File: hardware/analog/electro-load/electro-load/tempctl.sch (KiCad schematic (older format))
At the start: 25 parts, among them M1 Noctua NF-A14 5V, Q1 2N2222A, Q2 2N2222A, U4 LM358DR

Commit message: HW rev 1 of electronic load PCB.
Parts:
- removed R14, R17, R19: 1k, Resistor_SMD:R_0603_1608Metric, symbol Device:R_Small
- removed R15, R16: 10k POT, Potentiometer_SMD:Potentiometer_Bourns_3214W_Vertical, symbol Device:R_Small
- removed R18: 10k, Resistor_SMD:R_0603_1608Metric, symbol Device:R_Small
- removed R20: 3k3, Resistor_SMD:R_0603_1608Metric, symbol Device:R_Small
- removed TP4, TP5, TP8, TP9: TestPoint, athir:testpoint_probe, symbol Connector:TestPoint
- removed U4: LM358DR, digikey-footprints:SOIC-8_W3.9mm, symbol dk_Linear-Amplifiers-Instrumentation-OP-Amps-Buffer-Amps:LM358DR
- added C10, C11, C12, C13: 100n, Capacitor_SMD:C_0603_1608Metric, symbol Device:C_Small
- added R13, R5: 1k, Resistor_SMD:R_0603_1608Metric, symbol Device:R_Small
- added R4: 3k3 1%, Resistor_SMD:R_0603_1608Metric, symbol Device:R_Small
- added RV1, RV2, RV3, RV4: 10k POT, Potentiometer_THT:Potentiometer_Bourns_3296W_Vertical, symbol Device:R_POT
- added U3, U4: LMV321, Package_TO_SOT_SMD:SOT-23-5, symbol Amplifier_Operational:LMV321
- R10: value 10k -> 1k
- R12: value 3k3 -> 10k
- R7: value 10k POT -> 10k; footprint Potentiometer_SMD:Potentiometer_Bourns_3214W_Vertical -> Resistor_SMD:R_0603_1608Metric
- R8: value 10k POT -> 1k; footprint Potentiometer_SMD:Potentiometer_Bourns_3214W_Vertical -> Resistor_SMD:R_0603_1608Metric
- R9: value 1k -> 3k3 1%
- renumbered R13 to R14, TP6 to TP4, TP7 to TP5
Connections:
- wire segments 75 -> 97
- no-connect marks 0 -> 4
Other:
- note removed: "GAIN"

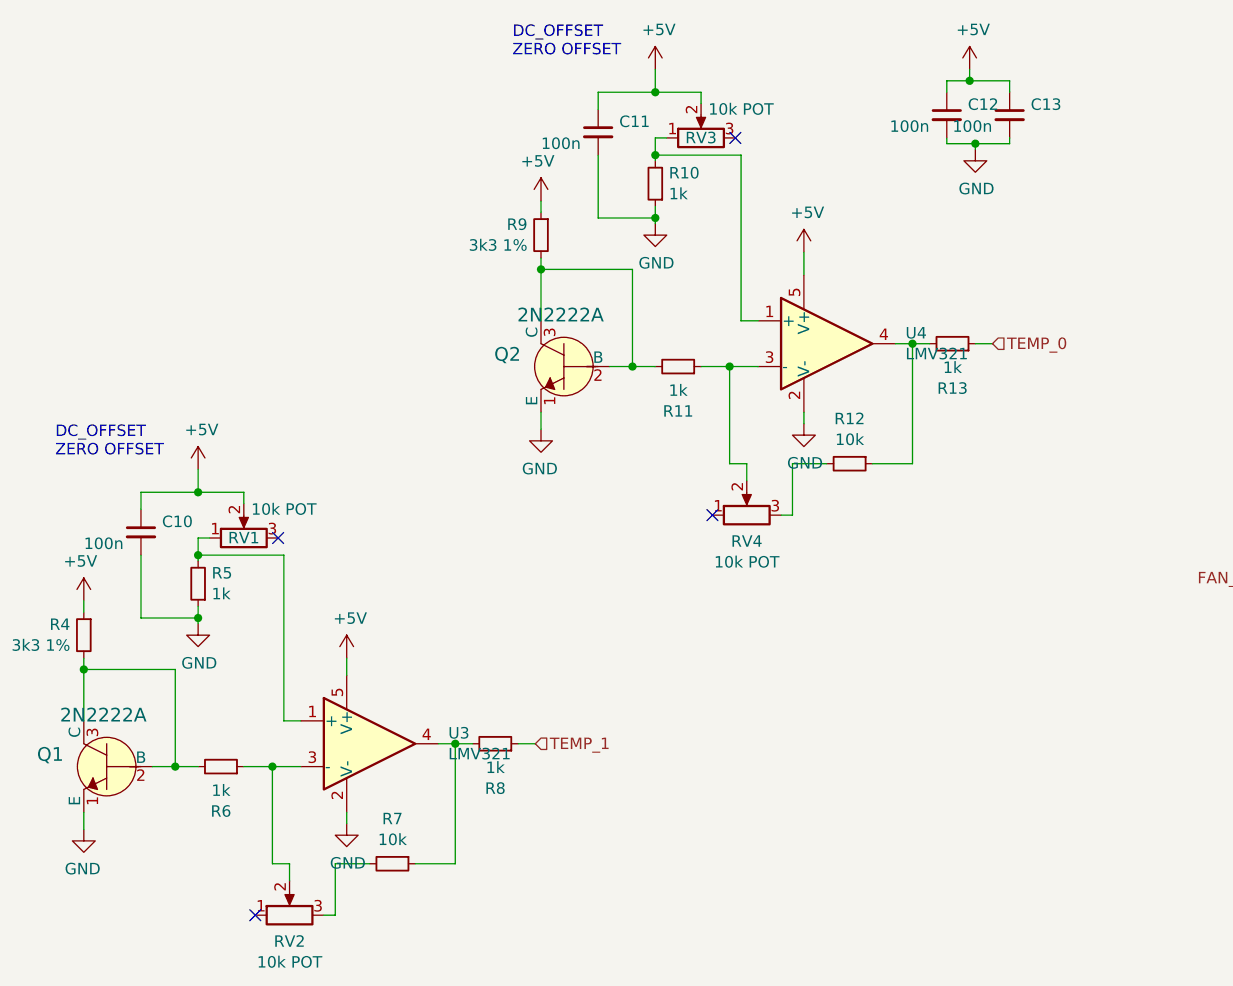
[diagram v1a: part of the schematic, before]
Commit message: Added voltage reference REF5020 datasheet
Started work on HW rev 2 of electro load and 5v-from-mains - rev 1 contained misaligned footprints.
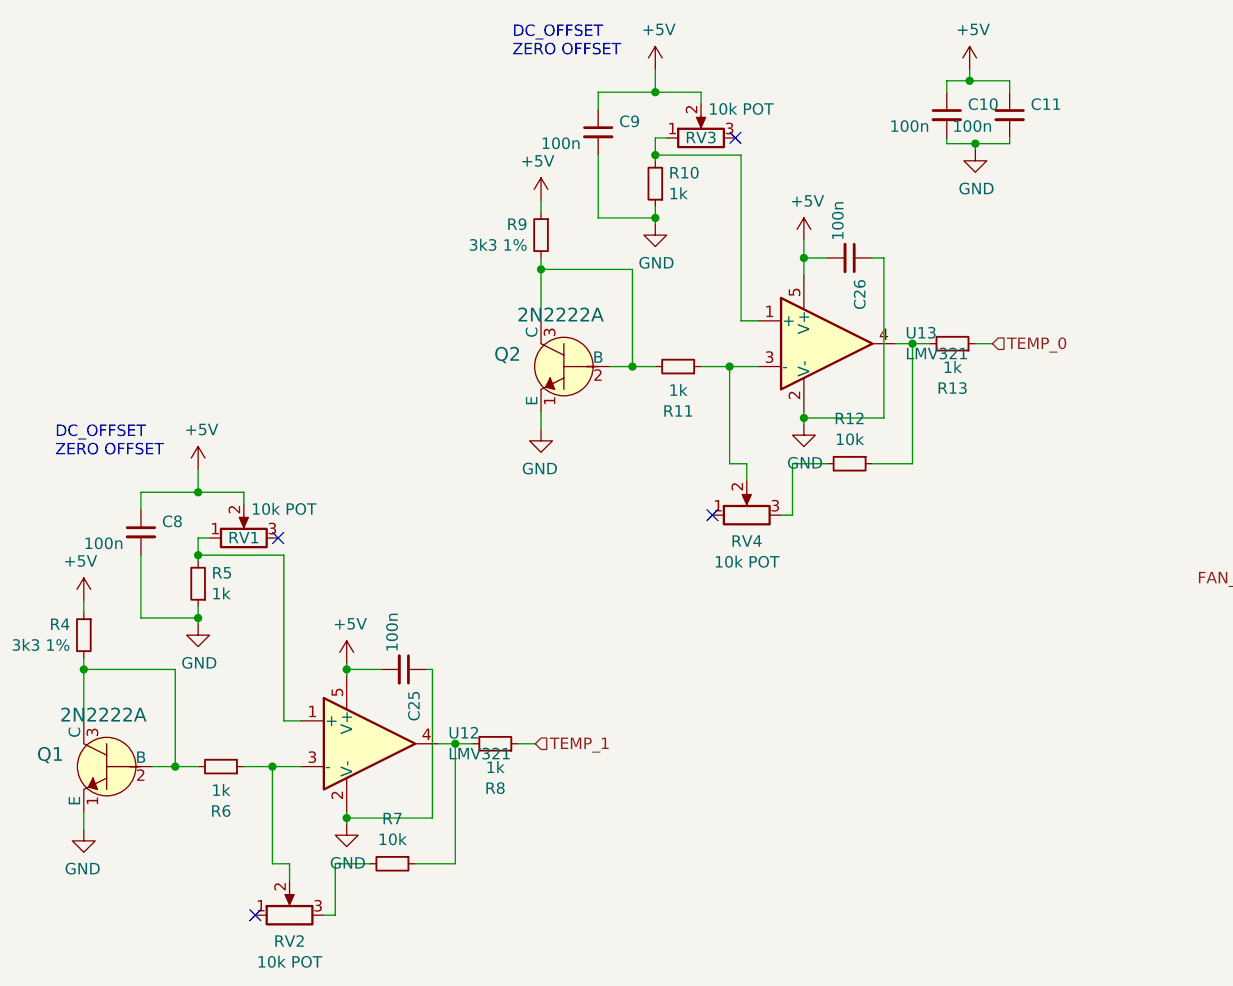
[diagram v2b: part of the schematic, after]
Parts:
- removed U3, U4: LMV321, Package_TO_SOT_SMD:SOT-23-5, symbol Amplifier_Operational:LMV321
- added C25, C26: 100n, Capacitor_SMD:C_0603_1608Metric, symbol Device:C_Small
- added U12, U13: LMV321, Package_TO_SOT_SMD:SOT-23-5, symbol Amplifier_Operational:LMV321
- renumbered C12 to C10, C13 to C11, C10 to C8, C11 to C9
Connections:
- net +5V: now also C25.2, C26.2, U12.5 (V+), U13.5 (V+)
- net GND: now also C25.1, C26.1, U12.2 (V-), U13.2 (V-)
- net at R10.2, RV3.1: now also U13.1 (+)
- net at R11.1, RV4.2: now also U13.3 (-)
- net at R12.1, R13.2: now also U13.4
- net at R5.2, RV1.1: now also U12.1 (+)
- net at R6.1, RV2.2: now also U12.3 (-)
- net at R7.1, R8.2: now also U12.4
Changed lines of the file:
@@
 P 7650 5150
 AR Path="/5E7E2279" Ref="#PWR?"  Part="1"
-AR Path="/5E789C0B/5E7E2279" Ref="#PWR034"  Part="1"
-F 0 "#PWR034" H 7650 5000 50  0001 C CNN
+AR Path="/5E789C0B/5E7E2279" Ref="#PWR029"  Part="1"
+F 0 "#PWR029" H 7650 5000 50  0001 C CNN
 F 1 "+5V" H 7665 5323 50  0000 C CNN
 F 2 "" H 7650 5150 50  0001 C CNN
@@
 P 7650 5725
 AR Path="/5E7E227F" Ref="#PWR?"  Part="1"
-AR Path="/5E789C0B/5E7E227F" Ref="#PWR035"  Part="1"
-F 0 "#PWR035" H 7650 5475 50  0001 C CNN
+AR Path="/5E789C0B/5E7E227F" Ref="#PWR030"  Part="1"
+F 0 "#PWR030" H 7650 5475 50  0001 C CNN
 F 1 "GND" H 7655 5552 50  0000 C CNN
 F 2 "" H 7650 5725 50  0001 C CNN
@@
 Wire Wire Line
 	6975 5600 7350 5600
-$Comp
-L Amplifier_Operational:LMV321 U4
-U 1 1 5EE66663
-P 4950 4575
-F 0 "U4" H 5294 4621 50  0000 L CNN
-F 1 "LMV321" H 5294 4530 50  0000 L CNN
-F 2 "Package_TO_SOT_SMD:SOT-23-5" H 4950 4575 50  0001 L CNN
-F 3 "http://www.ti.com/lit/ds/symlink/lmv324.pdf" H 4950 4575 50  0001 C CNN
-	1    4950 4575
-	1    0    0    -1
-$EndComp
 $Comp
 L dk_Transistors-Bipolar-BJT-Single:2N2222A Q?
@@
 P 3700 3950
 AR Path="/5EE6FAB4" Ref="#PWR?"  Part="1"
-AR Path="/5E789C0B/5EE6FAB4" Ref="#PWR026"  Part="1"
-F 0 "#PWR026" H 3700 3800 50  0001 C CNN
+AR Path="/5E789C0B/5EE6FAB4" Ref="#PWR023"  Part="1"
+F 0 "#PWR023" H 3700 3800 50  0001 C CNN
 F 1 "+5V" H 3715 4123 50  0000 C CNN
 F 2 "" H 3700 3950 50  0001 C CNN
@@
 	3700 3950 3700 4000
 $Comp
-L power:GND #PWR027
+L power:GND #PWR024
 U 1 1 5EE72CAB
 P 3700 4950
-F 0 "#PWR027" H 3700 4700 50  0001 C CNN
+F 0 "#PWR024" H 3700 4700 50  0001 C CNN
 F 1 "GND" H 3705 4777 50  0000 C CNN
 F 2 "" H 3700 4950 50  0001 C CNN
@@
 P 4200 4050
 AR Path="/5EE9863D" Ref="#PWR?"  Part="1"
-AR Path="/5E789C0B/5EE9863D" Ref="#PWR029"  Part="1"
-F 0 "#PWR029" H 4200 3800 50  0001 C CNN
+AR Path="/5E789C0B/5EE9863D" Ref="#PWR026"  Part="1"
+F 0 "#PWR026" H 4200 3800 50  0001 C CNN
 F 1 "GND" H 4205 3877 50  0000 C CNN
 F 2 "" H 4200 4050 50  0001 C CNN
@@
 P 4200 3375
 AR Path="/5EE9864C" Ref="#PWR?"  Part="1"
-AR Path="/5E789C0B/5EE9864C" Ref="#PWR028"  Part="1"
-F 0 "#PWR028" H 4200 3225 50  0001 C CNN
+AR Path="/5E789C0B/5EE9864C" Ref="#PWR025"  Part="1"
+F 0 "#PWR025" H 4200 3225 50  0001 C CNN
 F 1 "+5V" H 4215 3548 50  0000 C CNN
 F 2 "" H 4200 3375 50  0001 C CNN
@@
 	5675 4575 5600 4575
 $Comp
-L Device:C_Small C11
+L Device:C_Small C9
 U 1 1 5EEBC268
 P 3950 3650
-F 0 "C11" H 4042 3696 50  0000 L CNN
+F 0 "C9" H 4042 3696 50  0000 L CNN
 F 1 "100n" H 3700 3600 50  0000 L CNN
 F 2 "Capacitor_SMD:C_0603_1608Metric" H 3950 3650 50  0001 C CNN
@@
 	4400 3475 4200 3475
 NoConn ~ 4550 3675
-$Comp
-L Amplifier_Operational:LMV321 U3
-U 1 1 5EF00CA1
-P 2950 6325
-F 0 "U3" H 3294 6371 50  0000 L CNN
-F 1 "LMV321" H 3294 6280 50  0000 L CNN
-F 2 "Package_TO_SOT_SMD:SOT-23-5" H 2950 6325 50  0001 L CNN
-F 3 "http://www.ti.com/lit/ds/symlink/lmv324.pdf" H 2950 6325 50  0001 C CNN
-	1    2950 6325
-	1    0    0    -1
-$EndComp
 $Comp
 L dk_Transistors-Bipolar-BJT-Single:2N2222A Q?
@@
 P 1700 5700
 AR Path="/5EF00CCE" Ref="#PWR?"  Part="1"
-AR Path="/5E789C0B/5EF00CCE" Ref="#PWR020"  Part="1"
-F 0 "#PWR020" H 1700 5550 50  0001 C CNN
+AR Path="/5E789C0B/5EF00CCE" Ref="#PWR019"  Part="1"
+F 0 "#PWR019" H 1700 5550 50  0001 C CNN
 F 1 "+5V" H 1715 5873 50  0000 C CNN
 F 2 "" H 1700 5700 50  0001 C CNN
@@
 	1700 5700 1700 5750
 $Comp
-L power:GND #PWR021
+L power:GND #PWR020
 U 1 1 5EF00CD9
 P 1700 6700
-F 0 "#PWR021" H 1700 6450 50  0001 C CNN
+F 0 "#PWR020" H 1700 6450 50  0001 C CNN
 F 1 "GND" H 1705 6527 50  0000 C CNN
 F 2 "" H 1700 6700 50  0001 C CNN
@@
 P 2200 5800
 AR Path="/5EF00D0D" Ref="#PWR?"  Part="1"
-AR Path="/5E789C0B/5EF00D0D" Ref="#PWR023"  Part="1"
-F 0 "#PWR023" H 2200 5550 50  0001 C CNN
+AR Path="/5E789C0B/5EF00D0D" Ref="#PWR022"  Part="1"
+F 0 "#PWR022" H 2200 5550 50  0001 C CNN
 F 1 "GND" H 2205 5627 50  0000 C CNN
 F 2 "" H 2200 5800 50  0001 C CNN
@@
 P 2200 5125
 AR Path="/5EF00D1C" Ref="#PWR?"  Part="1"
-AR Path="/5E789C0B/5EF00D1C" Ref="#PWR022"  Part="1"
-F 0 "#PWR022" H 2200 4975 50  0001 C CNN
+AR Path="/5E789C0B/5EF00D1C" Ref="#PWR021"  Part="1"
+F 0 "#PWR021" H 2200 4975 50  0001 C CNN
 F 1 "+5V" H 2215 5298 50  0000 C CNN
 F 2 "" H 2200 5125 50  0001 C CNN
@@
 	3675 6325 3600 6325
 $Comp
-L Device:C_Small C10
+L Device:C_Small C8
 U 1 1 5EF00D2B
 P 1950 5400
-F 0 "C10" H 2042 5446 50  0000 L CNN
+F 0 "C8" H 2042 5446 50  0000 L CNN
 F 1 "100n" H 1700 5350 50  0000 L CNN
 F 2 "Capacitor_SMD:C_0603_1608Metric" H 1950 5400 50  0001 C CNN
@@
 Text HLabel 3675 6325 2    50   Input ~ 0
 TEMP_1
-$Comp
-L power:+5V #PWR030
-U 1 1 5E806CF4
-P 4850 4175
-F 0 "#PWR030" H 4850 4025 50  0001 C CNN
-F 1 "+5V" H 4865 4348 50  0000 C CNN
-F 2 "" H 4850 4175 50  0001 C CNN
-F 3 "" H 4850 4175 50  0001 C CNN
-	1    4850 4175
-	1    0    0    -1
-$EndComp
-Wire Wire Line
-	4850 4175 4850 4275
-$Comp
-L power:GND #PWR031
-U 1 1 5E809918
-P 4850 4925
-F 0 "#PWR031" H 4850 4675 50  0001 C CNN
-F 1 "GND" H 4855 4752 50  0000 C CNN
-F 2 "" H 4850 4925 50  0001 C CNN
-F 3 "" H 4850 4925 50  0001 C CNN
-	1    4850 4925
-	1    0    0    -1
-$EndComp
-Wire Wire Line
-	4850 4875 4850 4925
-$Comp
-L power:GND #PWR025
-U 1 1 5E80C416
-P 2850 6675
-F 0 "#PWR025" H 2850 6425 50  0001 C CNN
-F 1 "GND" H 2855 6502 50  0000 C CNN
-F 2 "" H 2850 6675 50  0001 C CNN
-F 3 "" H 2850 6675 50  0001 C CNN
-	1    2850 6675
-	1    0    0    -1
-$EndComp
-Wire Wire Line
-	2850 6675 2850 6625
-$Comp
-L power:+5V #PWR024
-U 1 1 5E8100D3
-P 2850 5950
-F 0 "#PWR024" H 2850 5800 50  0001 C CNN
-F 1 "+5V" H 2865 6123 50  0000 C CNN
-F 2 "" H 2850 5950 50  0001 C CNN
-F 3 "" H 2850 5950 50  0001 C CNN
-	1    2850 5950
-	1    0    0    -1
-$EndComp
-Wire Wire Line
-	2850 5950 2850 6025
 Text HLabel 5675 4575 2    50   Input ~ 0
 TEMP_0
 $Comp
-L Device:C_Small C12
+L Device:C_Small C10
 U 1 1 5E81574E
 P 5475 3575
-F 0 "C12" H 5567 3621 50  0000 L CNN
+F 0 "C10" H 5567 3621 50  0000 L CNN
 F 1 "100n" H 5225 3525 50  0000 L CNN
 F 2 "Capacitor_SMD:C_0603_1608Metric" H 5475 3575 50  0001 C CNN
@@
 P 5575 3375
 AR Path="/5E815D26" Ref="#PWR?"  Part="1"
-AR Path="/5E789C0B/5E815D26" Ref="#PWR032"  Part="1"
-F 0 "#PWR032" H 5575 3225 50  0001 C CNN
+AR Path="/5E789C0B/5E815D26" Ref="#PWR027"  Part="1"
+F 0 "#PWR027" H 5575 3225 50  0001 C CNN
 F 1 "+5V" H 5590 3548 50  0000 C CNN
 F 2 "" H 5575 3375 50  0001 C CNN
@@
 $EndComp
 $Comp
-L Device:C_Small C13
+L Device:C_Small C11
 U 1 1 5E816EA0
 P 5750 3575
-F 0 "C13" H 5842 3621 50  0000 L CNN
+F 0 "C11" H 5842 3621 50  0000 L CNN
 F 1 "100n" H 5500 3525 50  0000 L CNN
 F 2 "Capacitor_SMD:C_0603_1608Metric" H 5750 3575 50  0001 C CNN
@@
 Connection ~ 5575 3425
 $Comp
-L power:GND #PWR033
+L power:GND #PWR028
 U 1 1 5E81C942
 P 5600 3725
-F 0 "#PWR033" H 5600 3475 50  0001 C CNN
+F 0 "#PWR028" H 5600 3475 50  0001 C CNN
 F 1 "GND" H 5605 3552 50  0000 C CNN
 F 2 "" H 5600 3725 50  0001 C CNN
@@
 Text HLabel 6975 5600 0    50   Input ~ 0
 FAN_PWM
+$Comp
+L Amplifier_Operational:LMV321 U13
+U 1 1 5EA0DBAF
+P 4950 4575
+F 0 "U13" H 5294 4621 50  0000 L CNN
+F 1 "LMV321" H 5294 4530 50  0000 L CNN
+F 2 "Package_TO_SOT_SMD:SOT-23-5" H 4950 4575 50  0001 L CNN
+F 3 "http://www.ti.com/lit/ds/symlink/lmv324.pdf" H 4950 4575 50  0001 C CNN
+	1    4950 4575
+	1    0    0    -1
+$EndComp
+$Comp
+L Amplifier_Operational:LMV321 U12
+U 1 1 5EA1147F
+P 2950 6325
+F 0 "U12" H 3294 6371 50  0000 L CNN
+F 1 "LMV321" H 3294 6280 50  0000 L CNN
+F 2 "Package_TO_SOT_SMD:SOT-23-5" H 2950 6325 50  0001 L CNN
+F 3 "http://www.ti.com/lit/ds/symlink/lmv324.pdf" H 2950 6325 50  0001 C CNN
+	1    2950 6325
+	1    0    0    -1
+$EndComp
+$Comp
+L power:GND #PWR0101
+U 1 1 5EA1C6C9
+P 4850 4925
+F 0 "#PWR0101" H 4850 4675 50  0001 C CNN
+F 1 "GND" H 4855 4752 50  0000 C CNN
+F 2 "" H 4850 4925 50  0001 C CNN
+F 3 "" H 4850 4925 50  0001 C CNN
+	1    4850 4925
+	1    0    0    -1
+$EndComp
+Wire Wire Line
+	4850 4925 4850 4900
+$Comp
+L power:GND #PWR0102
+U 1 1 5EA1F791
+P 2850 6675
+F 0 "#PWR0102" H 2850 6425 50  0001 C CNN
+F 1 "GND" H 2855 6502 50  0000 C CNN
+F 2 "" H 2850 6675 50  0001 C CNN
+F 3 "" H 2850 6675 50  0001 C CNN
+	1    2850 6675
+	1    0    0    -1
+$EndComp
+Wire Wire Line
+	2850 6675 2850 6650
+$Comp
+L power:+5V #PWR0103
+U 1 1 5EA2384D
+P 2850 5975
+F 0 "#PWR0103" H 2850 5825 50  0001 C CNN
+F 1 "+5V" H 2865 6148 50  0000 C CNN
+F 2 "" H 2850 5975 50  0001 C CNN
+F 3 "" H 2850 5975 50  0001 C CNN
+	1    2850 5975
+	1    0    0    -1
+$EndComp
+Wire Wire Line
+	2850 5975 2850 6000
+$Comp
+L Device:C_Small C25
+U 1 1 5EA26CB2
+P 3100 6000
+F 0 "C25" H 3192 6046 50  0000 L CNN
+F 1 "100n" H 2850 5950 50  0000 L CNN
+F 2 "Capacitor_SMD:C_0603_1608Metric" H 3100 6000 50  0001 C CNN
+F 3 "~" H 3100 6000 50  0001 C CNN
+	1    3100 6000
+	0    1    1    0
+$EndComp
+Wire Wire Line
+	3000 6000 2850 6000
+Connection ~ 2850 6000
+Wire Wire Line
+	2850 6000 2850 6025
+Wire Wire Line
+	3200 6000 3225 6000
+Wire Wire Line
+	3225 6000 3225 6650
+Wire Wire Line
+	3225 6650 2850 6650
+Connection ~ 2850 6650
+Wire Wire Line
+	2850 6650 2850 6625
+$Comp
+L Device:C_Small C26
+U 1 1 5EA2E04F
+P 5050 4200
+F 0 "C26" H 5142 4246 50  0000 L CNN
+F 1 "100n" H 4800 4150 50  0000 L CNN
+F 2 "Capacitor_SMD:C_0603_1608Metric" H 5050 4200 50  0001 C CNN
+F 3 "~" H 5050 4200 50  0001 C CNN
+	1    5050 4200
+	0    1    1    0
+$EndComp
+$Comp
+L power:+5V #PWR0104
+U 1 1 5EA2F5F5
+P 4850 4125
+F 0 "#PWR0104" H 4850 3975 50  0001 C CNN
+F 1 "+5V" H 4865 4298 50  0000 C CNN
+F 2 "" H 4850 4125 50  0001 C CNN
+F 3 "" H 4850 4125 50  0001 C CNN
+	1    4850 4125
+	1    0    0    -1
+$EndComp
+Wire Wire Line
+	4850 4125 4850 4200
+Wire Wire Line
+	4950 4200 4850 4200
+Connection ~ 4850 4200
+Wire Wire Line
+	4850 4200 4850 4275
+Wire Wire Line
+	5150 4200 5200 4200
+Wire Wire Line
+	5200 4200 5200 4900
+Wire Wire Line
+	5200 4900 4850 4900
+Connection ~ 4850 4900
+Wire Wire Line
+	4850 4900 4850 4875
 $EndSCHEMATC
